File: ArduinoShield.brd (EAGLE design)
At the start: 64.8 x 77.5 mm, 10 parts

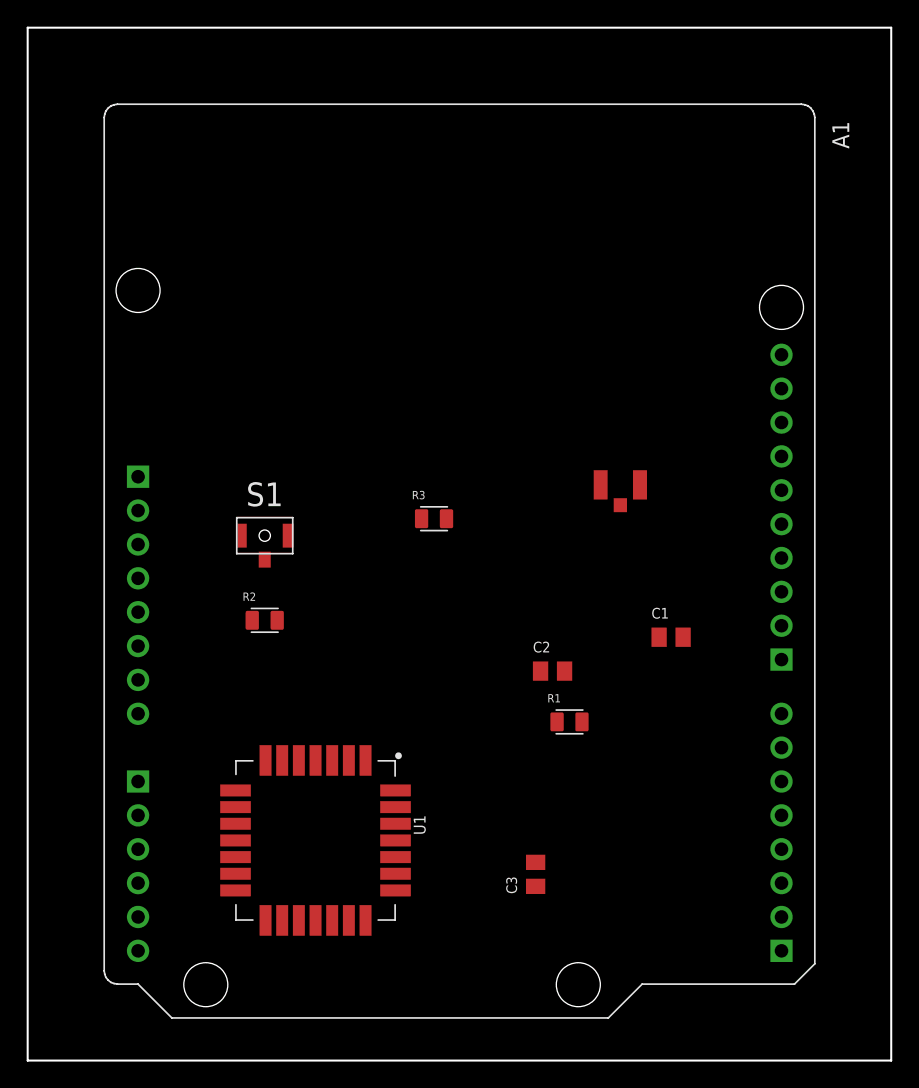
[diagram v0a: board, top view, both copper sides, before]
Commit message: Stubbed in lora
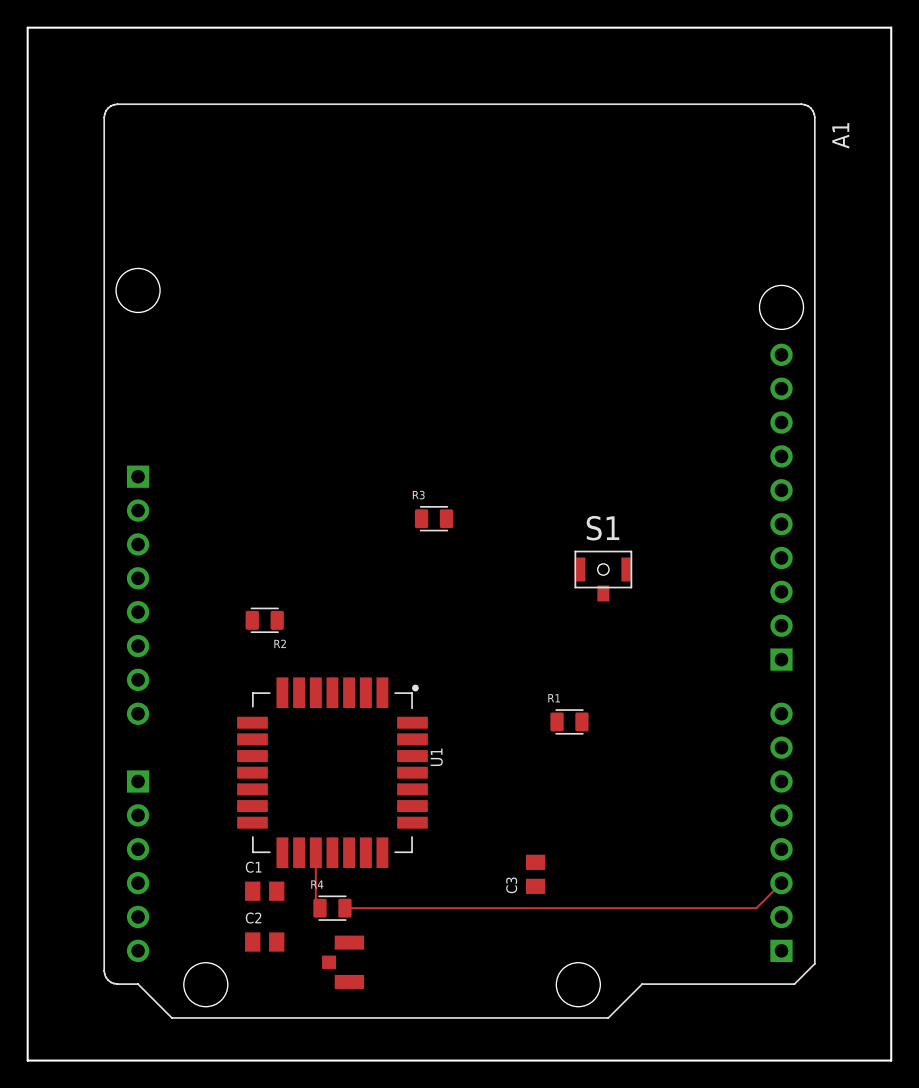
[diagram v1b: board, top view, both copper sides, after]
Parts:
- added R4: (no value), R0805:RESC2012X65N
- C1, C2: value LD051A121KAB2A -> (none)
- R3: value 2-2176053-0 -> (none)
- moved U$1 41.2 mm to (50.8, 20.1), turned to 270 degrees
- moved C1 35.9 mm to (44.5, 25.4)
- moved C2 29.6 mm to (44.5, 21.6)
- moved S1 25.5 mm to (69.8, 49.5)
- moved U1 5.24 mm to (49.5, 34.3)
- turned R2 to 180 degrees
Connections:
- removed net 3V3: A1.3V3
- removed net GND_1: A1.GND_1
- removed net GND_2: A1.GND_2
- removed net GND_3: A1.GND_3
- new net N$4: C3.1
- new net N$5: R4.1, U1.17
- new net RST: A1.D2, R4.2
- net GND: now also A1.GND_1, A1.GND_2, A1.GND_3; no longer C3.1
- net VCC: now also A1.3V3
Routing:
- net RST: track 0.00 -> 33.5 mm
- net N$5: track 0.00 -> 4.29 mm

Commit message: stubbed in i2c
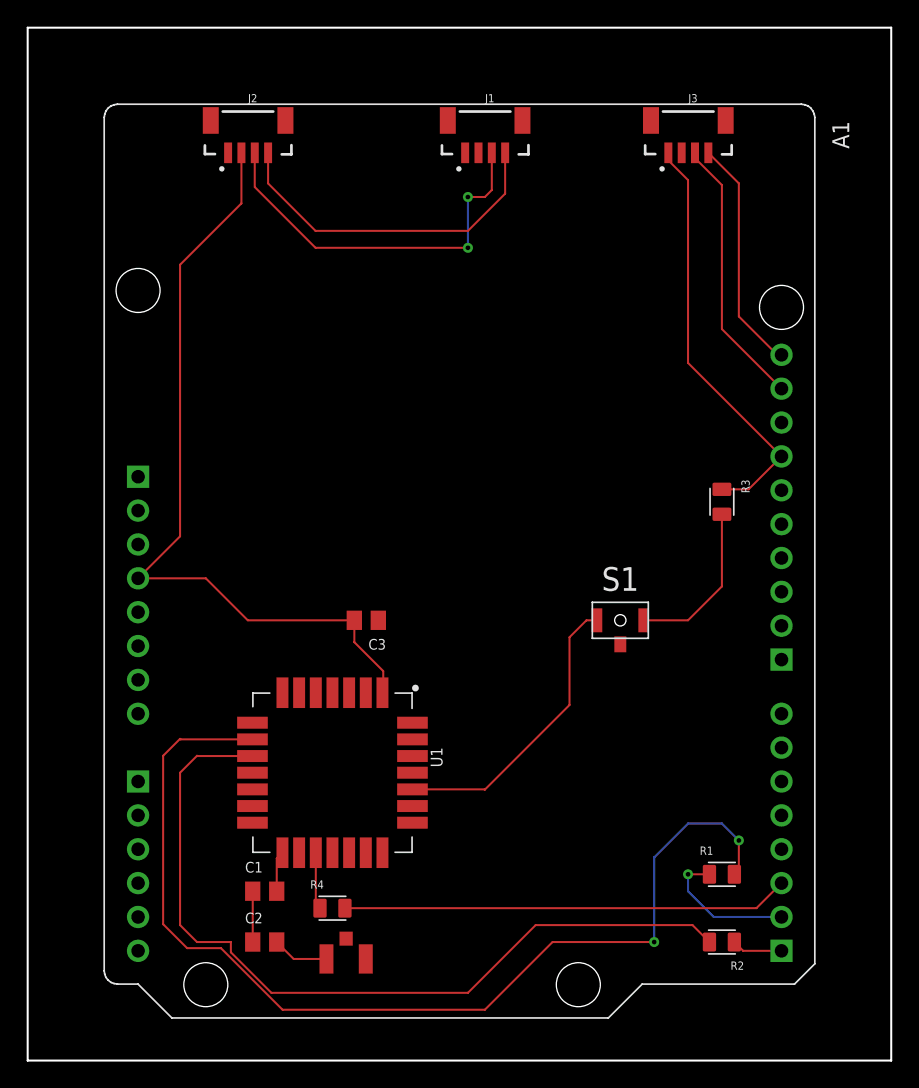
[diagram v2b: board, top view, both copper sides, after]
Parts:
- added J1, J2, J3: Vertical Qwiic Connector, SparkFun-Connectors:JST04_1MM_VERT
- moved R2 41.9 mm to (78.7, 21.6)
- moved C3 22.9 mm to (52.1, 45.7), turned to 180 degrees
- moved R3 21.6 mm to (78.7, 54.6), turned to 270 degrees
- moved R1 16.2 mm to (78.7, 26.7)
- moved S1 4.02 mm to (71.1, 45.7)
- moved U$1 0.35 mm to (50.6, 20.3), turned to 180 degrees
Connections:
- new net SCL: A1.A5(SCL), J1.4, J2.4, J3.4
- new net SDA: A1.A4(SDA), J1.3, J2.3, J3.3
- net GND: now also J1.1, J2.1, J3.1
- net VCC: now also J1.2, J2.2, J3.2
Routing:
- net N$2: track 0.00 -> 78.4 mm, vias 0 -> 2
- net N$1: track 0.00 -> 62.3 mm
- net VCC: track 0.00 -> 59.0 mm
- net SDA: track 0.00 -> 49.6 mm, vias 0 -> 2
- net SCL: track 0.00 -> 43.4 mm
- net GND: track 0.00 -> 42.9 mm
- net N$7: track 0.00 -> 22.1 mm
- net N$8: track 0.00 -> 12.3 mm
- net TX: track 0.00 -> 10.7 mm, vias 0 -> 1
- net RX: track 0.00 -> 3.81 mm

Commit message: one i2C
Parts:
- removed J2, J3: Vertical Qwiic Connector, SparkFun-Connectors:JST04_1MM_VERT
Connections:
- net GND: no longer J2.1, J3.1
- net SCL: no longer J2.4, J3.4
- net SDA: no longer J2.3, J3.3
- net VCC: no longer J2.2, J3.2
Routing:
- net GND: track 42.9 -> 16.6 mm
- net SDA: track 49.6 -> 38.2 mm, vias 2 -> 0
- net VCC: track 59.0 -> 70.1 mm
- net SCL: track 43.4 -> 35.3 mm
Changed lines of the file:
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@@
 <attribute name="NAME" x="60.976" y="84.57633125" size="0.6096" layer="25"/>
 <attribute name="PROD_ID" value="CONN-14483" x="60.96" y="80.01" size="1.778" layer="27" display="off"/>
-<attribute name="VALUE" x="60.976" y="78.71366875" size="0.6096" layer="27"/>
-</element>
-<element name="J2" library="SparkFun-Connectors" package="JST04_1MM_VERT" value="Vertical Qwiic Connector" x="43.18" y="80.01" smashed="yes">
-<attribute name="NAME" x="43.196" y="84.57633125" size="0.6096" layer="25"/>
-<attribute name="PROD_ID" value="CONN-14483" x="35.56" y="88.9" size="1.778" layer="27" display="off"/>
-<attribute name="VALUE" x="43.196" y="78.71366875" size="0.6096" layer="27"/>
-</element>
-<element name="J3" library="SparkFun-Connectors" package="JST04_1MM_VERT" value="Vertical Qwiic Connector" x="76.2" y="80.01" smashed="yes">
-<attribute name="NAME" x="76.216" y="84.57633125" size="0.6096" layer="25"/>
-<attribute name="PROD_ID" value="CONN-14483" x="68.58" y="87.63" size="1.778" layer="27" display="off"/>
-<attribute name="VALUE" x="76.216" y="78.71366875" size="0.6096" layer="27"/>
 </element>
 </elements>
@@
 <contactref element="A1" pad="3V3"/>
 <contactref element="J1" pad="2"/>
-<contactref element="J2" pad="2"/>
-<contactref element="J3" pad="2"/>
-<wire x1="42.702" y1="80.785" x2="42.702" y2="76.992" width="0.1524" layer="1"/>
-<wire x1="42.702" y1="76.992" x2="38.1" y2="72.39" width="0.1524" layer="1"/>
-<wire x1="38.1" y1="72.39" x2="38.1" y2="52.0192" width="0.1524" layer="1"/>
-<wire x1="38.1" y1="52.0192" x2="34.9504" y2="48.8696" width="0.1524" layer="1"/>
+<wire x1="38.1" y1="52.0192" x2="38.1" y2="62.23" width="0.1524" layer="1"/>
+<wire x1="34.9504" y1="48.8696" x2="38.1" y2="52.0192" width="0.1524" layer="1"/>
 <wire x1="34.9504" y1="48.8696" x2="40.0304" y2="48.8696" width="0.1524" layer="1"/>
 <wire x1="40.0304" y1="48.8696" x2="43.18" y2="45.72" width="0.1524" layer="1"/>
@@
 <wire x1="53.34" y1="41.91" x2="53.34" y2="40.35" width="0.1524" layer="1"/>
 <wire x1="53.34" y1="40.35" x2="53.28" y2="40.29" width="0.1524" layer="1"/>
-<wire x1="60.482" y1="80.785" x2="75.722" y2="80.785" width="0" layer="19" extent="1-1"/>
-<wire x1="42.702" y1="80.785" x2="60.482" y2="80.785" width="0" layer="19" extent="1-1"/>
+<wire x1="38.1" y1="62.23" x2="52.07" y2="76.2" width="0.1524" layer="1"/>
+<wire x1="52.07" y1="76.2" x2="58.42" y2="76.2" width="0.1524" layer="1"/>
+<wire x1="58.42" y1="76.2" x2="60.482" y2="78.262" width="0.1524" layer="1"/>
+<wire x1="60.482" y1="78.262" x2="60.482" y2="80.785" width="0.1524" layer="1"/>
 </signal>
 <signal name="RX">
@@
 <contactref element="U1" pad="22"/>
 <contactref element="J1" pad="1"/>
-<contactref element="J2" pad="1"/>
-<contactref element="J3" pad="1"/>
 <wire x1="49.0786" y1="20.32" x2="46.62" y2="20.32" width="0.1524" layer="1"/>
 <wire x1="46.62" y1="20.32" x2="45.35" y2="21.59" width="0.1524" layer="1"/>
-<wire x1="83.2104" y1="58.0136" x2="76.2" y2="65.024" width="0.1524" layer="1"/>
-<wire x1="76.2" y1="65.024" x2="76.2" y2="78.74" width="0.1524" layer="1"/>
-<wire x1="76.2" y1="78.74" x2="74.722" y2="80.218" width="0.1524" layer="1"/>
-<wire x1="74.722" y1="80.218" x2="74.722" y2="80.785" width="0.1524" layer="1"/>
 <wire x1="45.35" y1="25.4" x2="45.35" y2="27.86" width="0.1524" layer="1"/>
 <wire x1="45.35" y1="27.86" x2="45.78" y2="28.29" width="0.1524" layer="1"/>
@@
 <wire x1="80.7418" y1="55.545" x2="78.74" y2="55.545" width="0.1524" layer="1"/>
 <wire x1="43.55" y1="25.4" x2="43.55" y2="21.59" width="0.1524" layer="1"/>
-<wire x1="74.722" y1="80.785" x2="59.482" y2="80.785" width="0" layer="19" extent="1-1"/>
-<wire x1="41.702" y1="80.785" x2="59.482" y2="80.785" width="0" layer="19" extent="1-1"/>
+<wire x1="78.74" y1="55.545" x2="59.482" y2="80.785" width="0" layer="19" extent="1-1"/>
 <wire x1="52.03" y1="40.29" x2="78.74" y2="55.545" width="0" layer="19" extent="1-1"/>
 <wire x1="55.53" y1="30.54" x2="52.03" y2="40.29" width="0" layer="19" extent="1-1"/>
@@
 <contactref element="A1" pad="A4(SDA)"/>
 <contactref element="J1" pad="3"/>
-<contactref element="J2" pad="3"/>
-<contactref element="J3" pad="3"/>
 <wire x1="78.74" y1="67.564" x2="83.2104" y2="63.0936" width="0.1524" layer="1"/>
 <wire x1="78.74" y1="78.3687125" x2="78.74" y2="67.564" width="0.1524" layer="1"/>
-<wire x1="76.722" y1="80.785" x2="76.52285625" y2="80.58585625" width="0.1524" layer="1"/>
-<wire x1="76.52285625" y1="80.58585625" x2="78.74" y2="78.3687125" width="0.1524" layer="1"/>
-<wire x1="43.702" y1="80.785" x2="43.702" y2="78.218" width="0.1524" layer="1"/>
-<wire x1="43.702" y1="78.218" x2="48.26" y2="73.66" width="0.1524" layer="1"/>
-<wire x1="48.26" y1="73.66" x2="59.69" y2="73.66" width="0.1524" layer="1"/>
-<via x="59.69" y="73.66" extent="1-16" drill="0.35"/>
-<via x="59.69" y="77.47" extent="1-16" drill="0.35"/>
-<wire x1="61.482" y1="80.785" x2="61.482" y2="77.992" width="0.1524" layer="1"/>
-<wire x1="61.482" y1="77.992" x2="60.96" y2="77.47" width="0.1524" layer="1"/>
-<wire x1="60.96" y1="77.47" x2="59.69" y2="77.47" width="0.1524" layer="1"/>
-<wire x1="59.69" y1="77.47" x2="59.69" y2="73.66" width="0.1524" layer="16"/>
-<wire x1="61.482" y1="80.785" x2="76.722" y2="80.785" width="0" layer="19" extent="1-1"/>
+<wire x1="75.8287125" y1="81.28" x2="78.74" y2="78.3687125" width="0.1524" layer="1"/>
+<wire x1="61.482" y1="80.785" x2="61.482" y2="79.488" width="0.1524" layer="1"/>
+<wire x1="61.482" y1="79.488" x2="62.23" y2="78.74" width="0.1524" layer="1"/>
+<wire x1="62.23" y1="78.74" x2="63.5" y2="78.74" width="0.1524" layer="1"/>
+<wire x1="63.5" y1="78.74" x2="66.04" y2="81.28" width="0.1524" layer="1"/>
+<wire x1="66.04" y1="81.28" x2="75.8287125" y2="81.28" width="0.1524" layer="1"/>
 </signal>
 <signal name="SCL">
 <contactref element="A1" pad="A5(SCL)"/>
 <contactref element="J1" pad="4"/>
-<contactref element="J2" pad="4"/>
-<contactref element="J3" pad="4"/>
 <wire x1="83.2104" y1="65.6336" x2="82.8883375" y2="65.6336" width="0.1524" layer="1"/>
 <wire x1="82.8883375" y1="65.6336" x2="80.01" y2="68.5119375" width="0.1524" layer="1"/>
-<wire x1="80.01" y1="68.5119375" x2="80.01" y2="78.497" width="0.1524" layer="1"/>
-<wire x1="80.01" y1="78.497" x2="77.722" y2="80.785" width="0.1524" layer="1"/>
-<wire x1="44.702" y1="80.785" x2="44.702" y2="78.488" width="0.1524" layer="1"/>
-<wire x1="44.702" y1="78.488" x2="48.26" y2="74.93" width="0.1524" layer="1"/>
-<wire x1="48.26" y1="74.93" x2="59.69" y2="74.93" width="0.1524" layer="1"/>
-<wire x1="59.69" y1="74.93" x2="62.482" y2="77.722" width="0.1524" layer="1"/>
-<wire x1="62.482" y1="77.722" x2="62.482" y2="80.785" width="0.1524" layer="1"/>
-<wire x1="62.482" y1="80.785" x2="77.722" y2="80.785" width="0" layer="19" extent="1-1"/>
+<wire x1="80.01" y1="68.5119375" x2="80.01" y2="80.01" width="0.1524" layer="1"/>
+<wire x1="80.01" y1="80.01" x2="77.47" y2="82.55" width="0.1524" layer="1"/>
+<wire x1="77.47" y1="82.55" x2="65.0452875" y2="82.55" width="0.1524" layer="1"/>
+<wire x1="63.2066875" y1="80.7114" x2="62.5556" y2="80.7114" width="0.1524" layer="1"/>
+<wire x1="62.5556" y1="80.7114" x2="62.482" y2="80.785" width="0.1524" layer="1"/>
+<wire x1="65.0452875" y1="82.55" x2="63.2066875" y2="80.7114" width="0.1524" layer="1"/>
 </signal>
 </signals>
